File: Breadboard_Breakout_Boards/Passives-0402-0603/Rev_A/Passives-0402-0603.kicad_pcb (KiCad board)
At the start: 2 copper layers, 9.9 x 20.1 mm, 10 parts, among them J1 Conn_01x08, J2 Conn_01x08

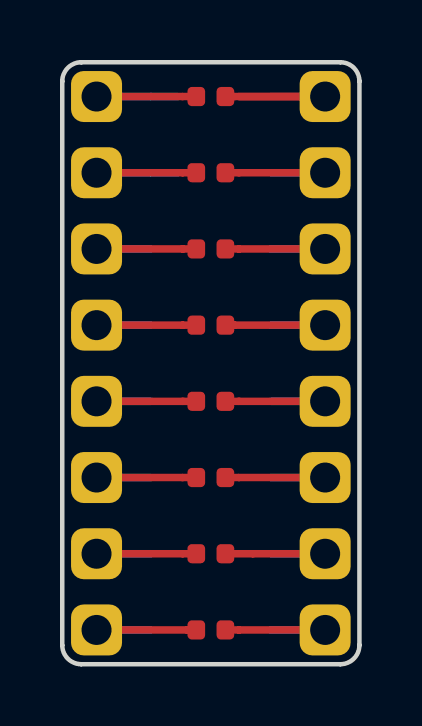
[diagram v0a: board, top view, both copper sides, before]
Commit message: Added 0402 / 0603 passives breakout
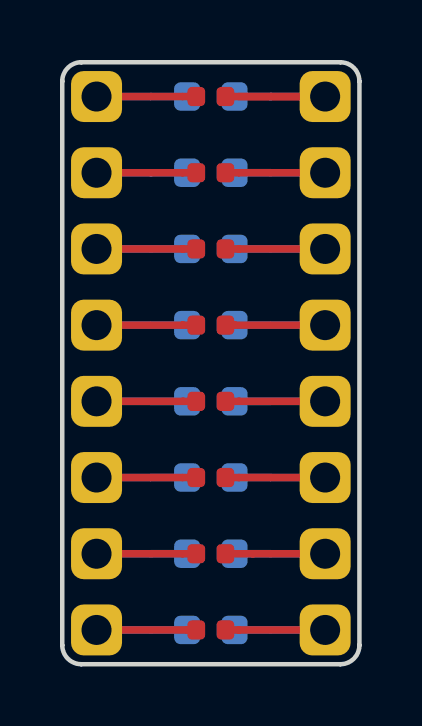
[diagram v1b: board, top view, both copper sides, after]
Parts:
- added R10: R, SA_Resistors_SMD:R_0603_1608M, B.Cu at (125.7, 66.0)
- added R11: R, SA_Resistors_SMD:R_0603_1608M, B.Cu at (125.7, 68.6)
- added R12: R, SA_Resistors_SMD:R_0603_1608M, B.Cu at (125.7, 71.1)
- added R13: R, SA_Resistors_SMD:R_0603_1608M, B.Cu at (125.7, 73.7)
- added R14: R, SA_Resistors_SMD:R_0603_1608M, B.Cu at (125.7, 76.2)
- added R15: R, SA_Resistors_SMD:R_0603_1608M, B.Cu at (125.7, 78.7)
- added R16: R, SA_Resistors_SMD:R_0603_1608M, B.Cu at (125.7, 81.3)
- added R9: R, SA_Resistors_SMD:R_0603_1608M, B.Cu at (125.7, 63.5)
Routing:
- net /8: track 5.13 -> 6.35 mm
- net /7: track 5.13 -> 6.35 mm
- net /6: track 5.13 -> 6.35 mm
- net /5: track 5.13 -> 6.35 mm
- net /4: track 5.13 -> 6.35 mm
- net /3: track 5.13 -> 6.35 mm
- net /2: track 5.13 -> 6.35 mm
- net /1: track 8.01 -> 9.22 mm
- net /9: track 5.14 -> 6.35 mm
- net /14: track 5.14 -> 6.35 mm
- net /13: track 5.14 -> 6.35 mm
- net /12: track 5.14 -> 6.35 mm
- net /11: track 5.14 -> 6.35 mm
- net /10: track 5.14 -> 6.35 mm
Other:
- net class Default: trace_width 0.1524 -> 0.254
- rule trace_min: 0.1524 -> 0.254
